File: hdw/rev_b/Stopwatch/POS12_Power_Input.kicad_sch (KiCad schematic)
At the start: 18 parts, among them J201 +12V IN

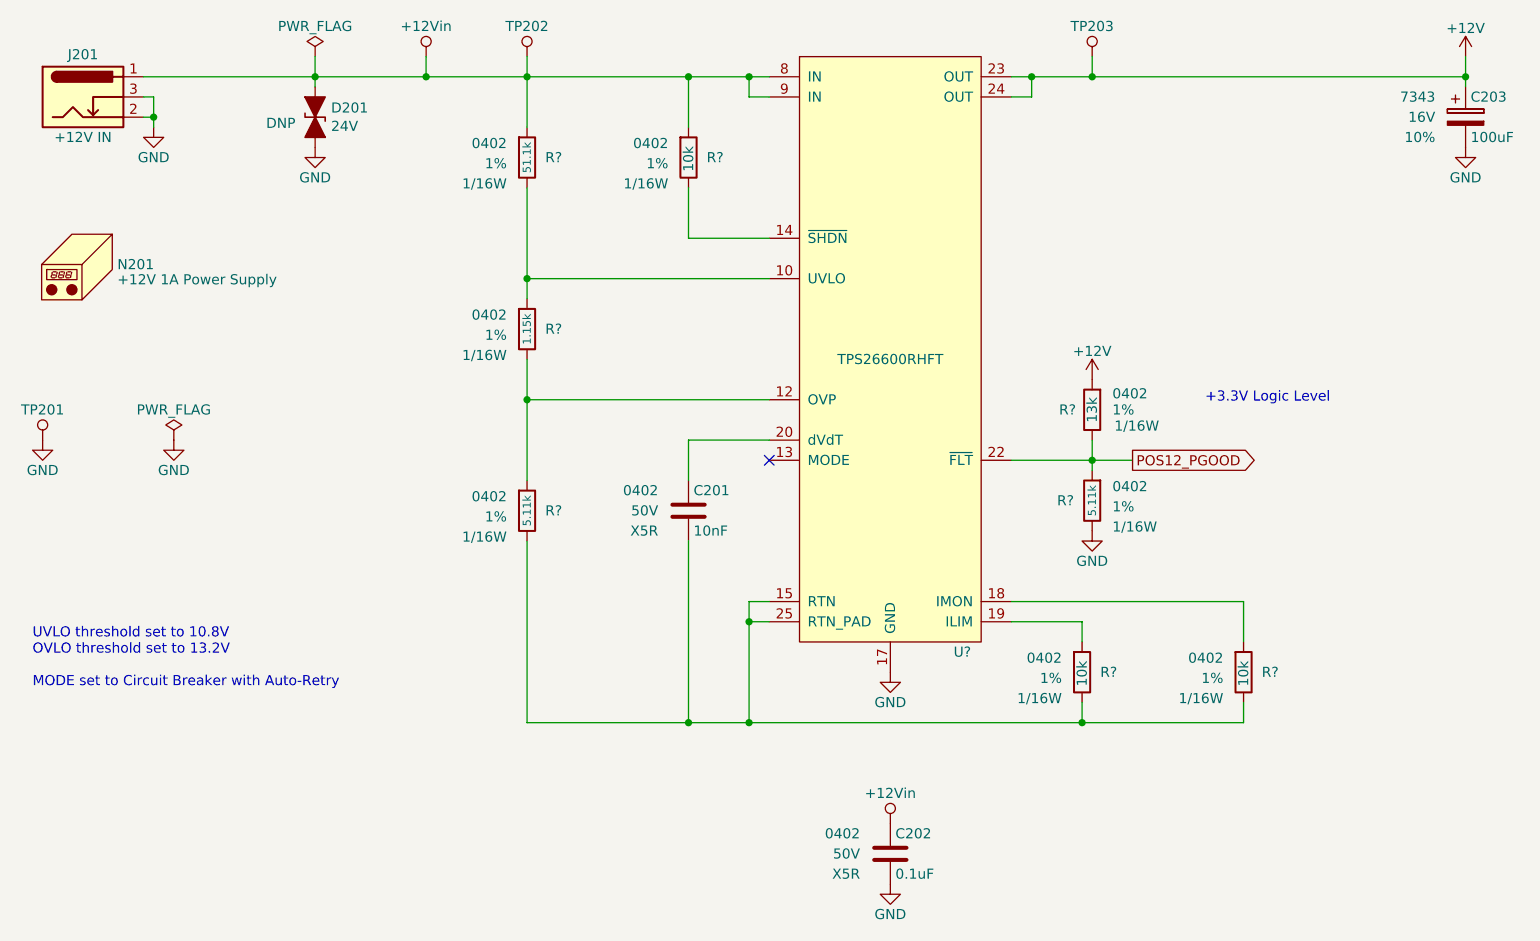
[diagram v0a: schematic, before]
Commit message: ported rev b to kicad 8
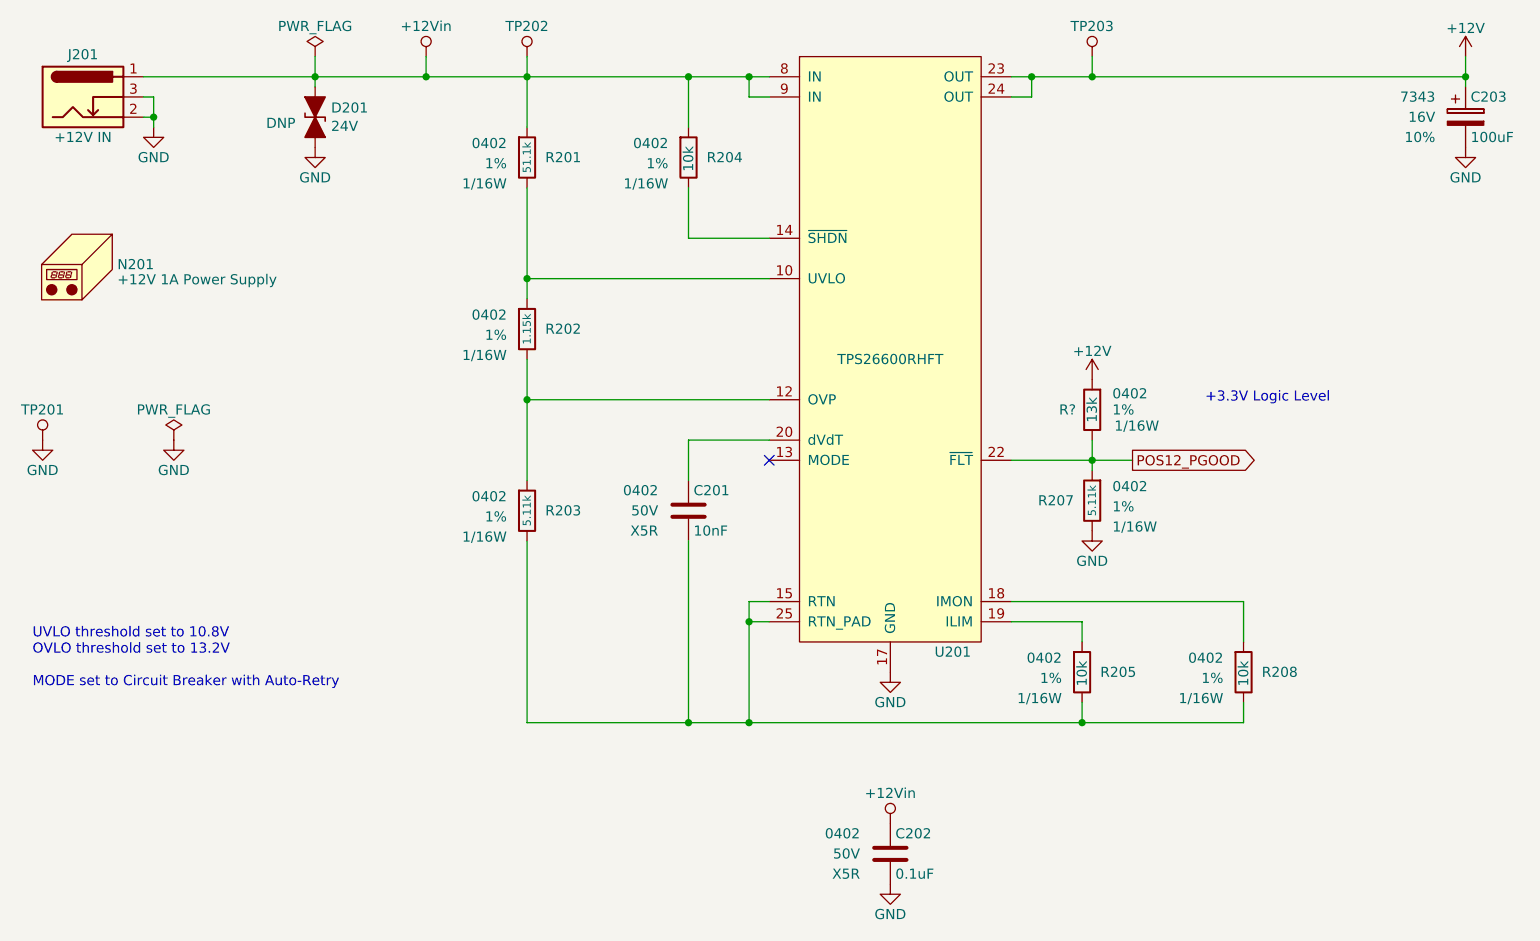
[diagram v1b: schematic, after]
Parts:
- gave numbers to parts that had none: 8
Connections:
- net at U201.12 (OVP): now also R202.2, R203.1

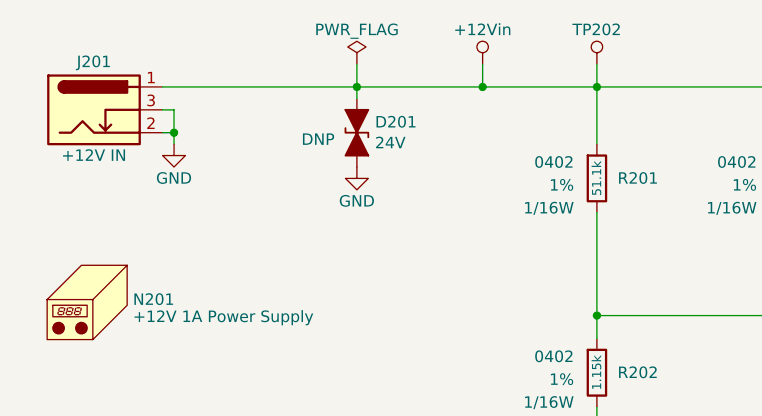
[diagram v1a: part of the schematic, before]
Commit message: integrated SC70 gates
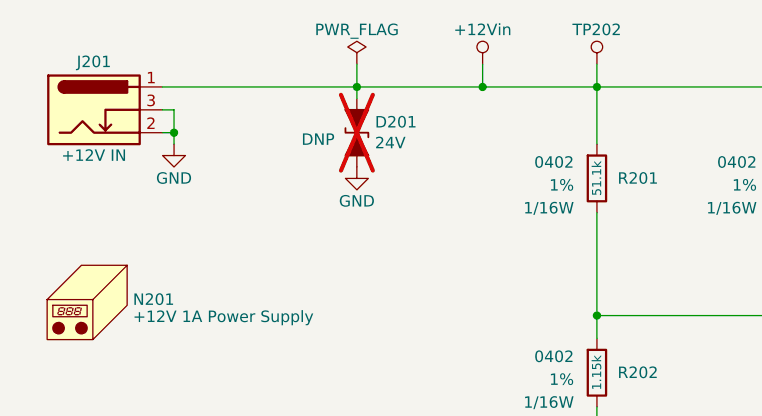
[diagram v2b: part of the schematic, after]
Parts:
- D201: now not fitted
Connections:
- net at U201.12 (OVP): now also R202.2, R203.1
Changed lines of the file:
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@@
 		(in_bom yes)
 		(on_board yes)
-		(dnp no)
+		(dnp yes)
 		(property "Reference" "D201"
 			(at 71.8566 61.0616 90)

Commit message: finished rev B PCB
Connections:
- net at U201.12 (OVP): now also R202.2, R203.1
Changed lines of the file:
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@@
 	(title_block
 		(title "Stopwatch")
-		(date "2024-01-11")
-		(rev "A")
+		(date "2024-04-28")
+		(rev "B")
 		(company "Drew Maatman")
 	)
